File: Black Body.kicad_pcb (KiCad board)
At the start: 2 copper layers, 55.5 x 53.8 mm, 36 parts, among them IC2 MCP96L00T-E_MX, J1 53307-2471, J3 Conn_01x04, J4 MX150_02x08_RightAngle

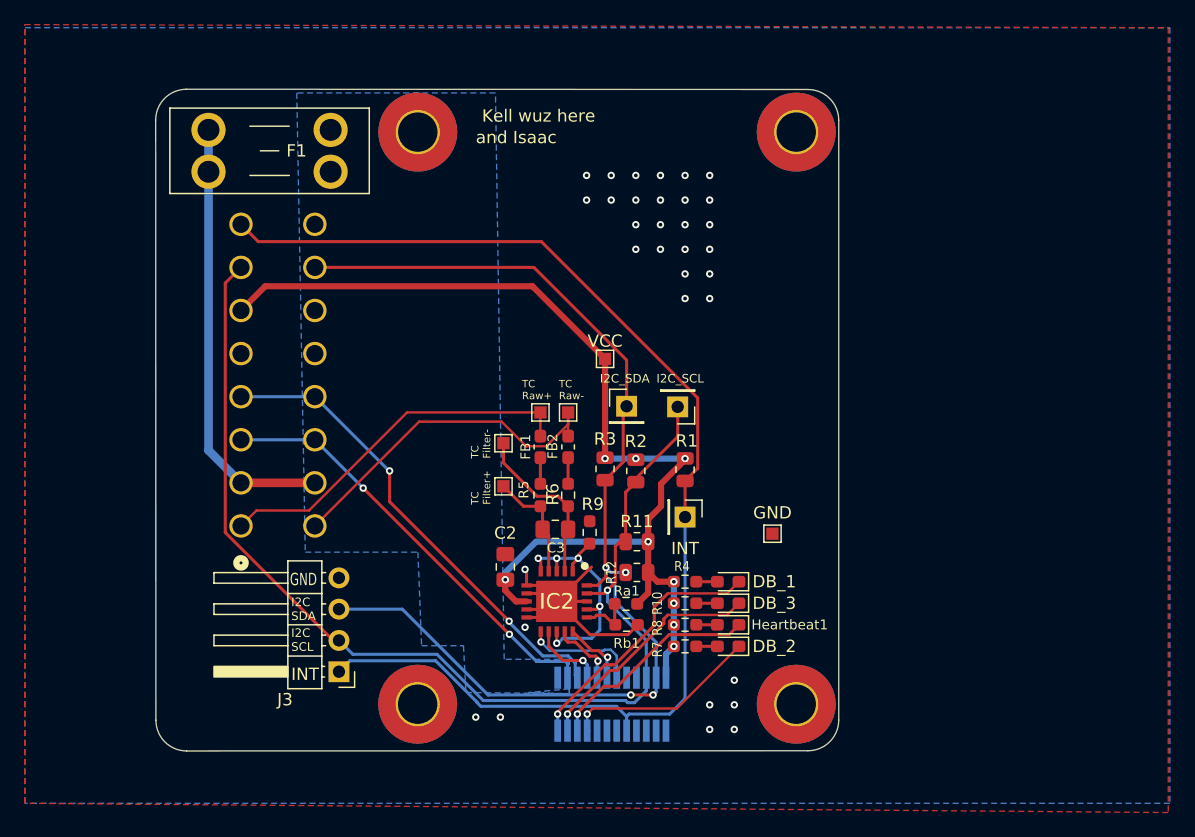
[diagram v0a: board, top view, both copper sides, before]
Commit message: swap from mx150 to nanofit
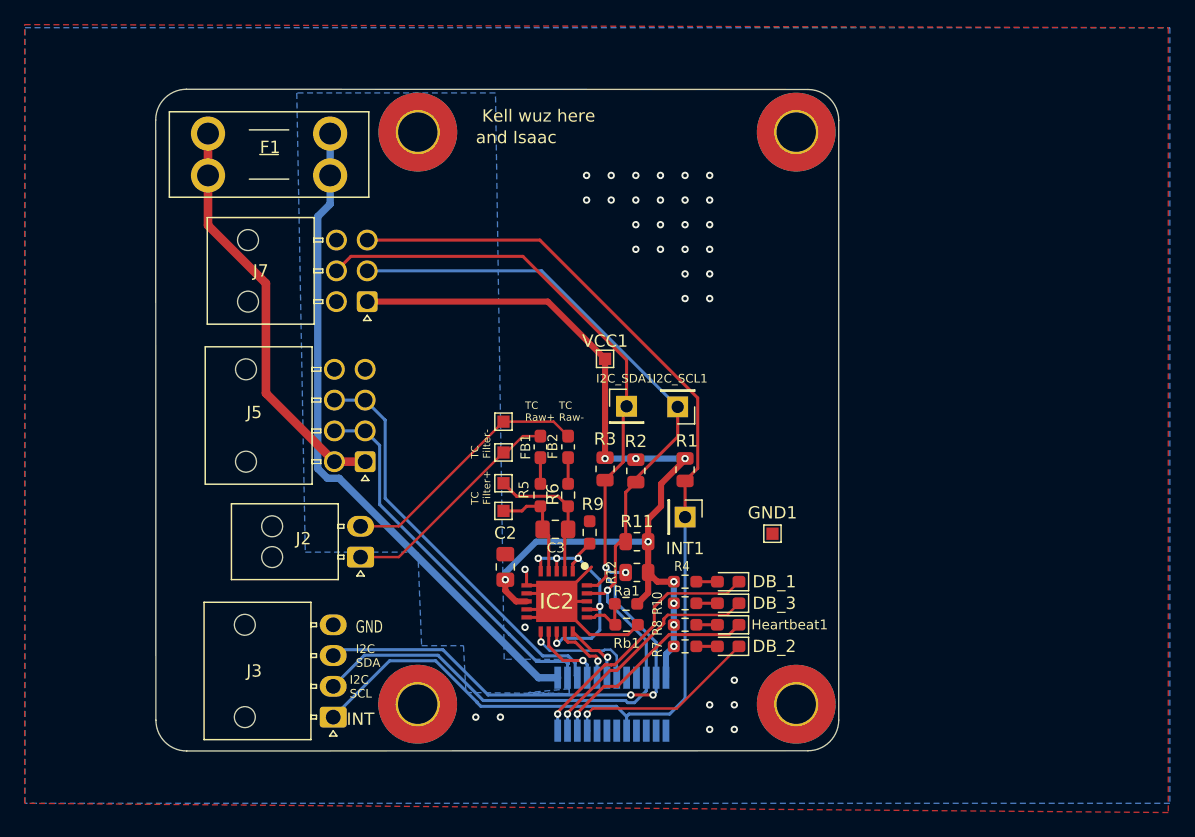
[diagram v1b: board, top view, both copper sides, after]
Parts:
- removed F1: 0.5, Fuse:Fuseholder_Blade_Mini_Keystone_3568
- removed J4: MX150_02x08_RightAngle, UTSVT-Conn:CONN_SD-75900-001_2X08_MOL
- added F2: 0.5, Fuse:Fuseholder_Blade_Mini_Keystone_3568, F.Cu at (78.2, 70.6)
- added J2: Conn_01x02, Connector_Molex:Molex_Nano-Fit_105313-xx02_1x02_P2.50mm_Horizontal, F.Cu at (90.6, 105.0)
- added J5: Conn_02x04_Top_Bottom, Connector_Molex:Molex_Nano-Fit_105314-xx08_2x04_P2.50mm_Horizontal, F.Cu at (91.0, 97.2)
- added J7: Conn_02x03_Top_Bottom, Connector_Molex:Molex_Nano-Fit_105314-xx06_2x03_P2.50mm_Horizontal, F.Cu at (91.2, 84.2)
- J3: footprint Connector_PinHeader_2.54mm:PinHeader_1x04_P2.54mm_Horizontal -> Connector_Molex:Molex_Nano-Fit_105313-xx04_1x04_P2.50mm_Horizontal
- moved TP_TC_2 5.30 mm to (102.2, 94.0), turned to 90 degrees
- moved TP_TC_1 4.42 mm to (102.2, 96.5), turned to -90 degrees
- moved J3 3.72 mm to (88.4, 118.0)
- moved TP_TC_F_2 3.25 mm to (102.2, 99.0)
- moved TP_TC_F_1 2.00 mm to (102.2, 101.2)
- renumbered GND to GND1, I2C_SCL to I2C_SCL1, I2C_SDA to I2C_SDA1, INT to INT1, VCC to VCC1
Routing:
- net +24V: track 0.00 -> 54.1 mm
- net +3V3: track 87.8 -> 76.2 mm
- net /Temp+: track 30.1 -> 18.7 mm
- net /INT: track 99.9 -> 91.1 mm
- net /Temp-: track 28.5 -> 20.9 mm
- net /CAN_L: track 38.9 -> 33.4 mm, vias 2 -> 0
- net /CAN_H: track 35.2 -> 30.7 mm, vias 2 -> 0
- net /I2C1_SCL: track 92.1 -> 88.0 mm
- net /temp: track 35.8 -> 33.4 mm
- net Net-(IC2-VIN+): track 13.7 -> 11.4 mm
- net /I2C1_SDA: track 91.2 -> 89.6 mm
- net Net-(IC2-VIN-): track 9.33 -> 8.82 mm
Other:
- board text added: "F1"

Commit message: Updated KiCad Sharepoint
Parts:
- moved F2 31.5 mm to (95.3, 97.1), turned to 90 degrees
- moved FB2 12.4 mm to (97.0, 102.5), turned to 0 degrees
- moved FB1 12.2 mm to (97.0, 105.0), turned to 0 degrees
- moved TP_TC_2 11.9 mm to (93.9, 102.5)
- moved TP_TC_1 11.9 mm to (94.0, 105.0)
- moved TP_TC_F_1 8.27 mm to (96.9, 107.6)
- moved R6 7.27 mm to (100.7, 102.5), turned to 180 degrees
- moved R5 6.82 mm to (100.7, 105.0), turned to 180 degrees
- moved TP_TC_F_2 5.64 mm to (107.6, 97.2)
- moved DB_1 5.33 mm to (120.5, 112.3)
- moved R4 5.33 mm to (117.0, 112.3)
- moved DB_2 5.10 mm to (120.5, 107.2)
- moved R7 5.10 mm to (117.0, 107.2)
- moved R11 3.71 mm to (112.8, 107.5)
- moved C2 2.92 mm to (101.6, 108.6), turned to 0 degrees
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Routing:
- net +24V: track 54.1 -> 1.55 mm
- net +3V3: track 76.2 -> 50.2 mm, vias 9 -> 4
- net /I2C1_SDA: track 89.6 -> 73.6 mm, vias 4 -> 3
- net /Temp-: track 20.9 -> 5.28 mm
- net /I2C1_SCL: track 88.0 -> 73.5 mm
- net GND: track 20.9 -> 7.12 mm, vias 33 -> 30
- net /Temp+: track 18.7 -> 5.19 mm
- net /DB_Conn_2: track 16.1 -> 24.3 mm
- net Net-(IC2-VIN-): track 8.82 -> 14.2 mm
- net /Heartbeat: track 17.5 -> 22.7 mm
- net /DB_Conn_1: track 21.5 -> 18.5 mm
- net Net-(DB_3-A): track 1.96 -> 0.00 mm
- net Net-(IC2-ADDR): track 4.50 -> 2.68 mm
- net /DB_Conn_3: track 19.3 -> 21.0 mm
- net Net-(DB_2-A): track 1.71 -> 0.00 mm
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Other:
- board text added: "VCC"
